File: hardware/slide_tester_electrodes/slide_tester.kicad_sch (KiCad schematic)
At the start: 17 parts, among them J1 USB_A_Stacked, J2 Conn_01x01_Male, J3 Conn_01x01_Male, Q1 C32725, Q2 C32725, Q3 C32725

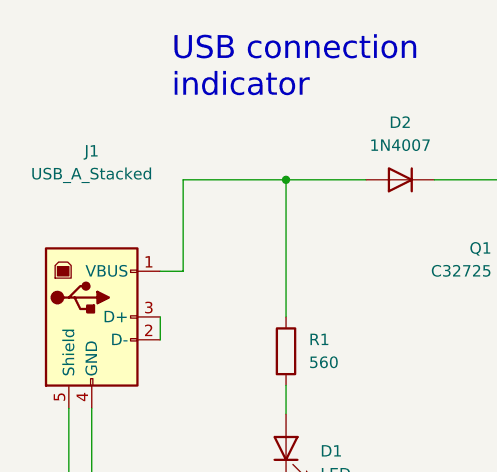
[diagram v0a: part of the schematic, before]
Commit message: Add description, figures
Add gitignore and delete back-ups
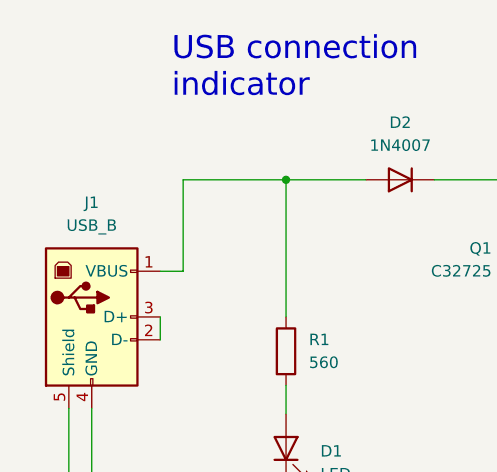
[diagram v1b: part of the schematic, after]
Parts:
- J1: value USB_A_Stacked -> USB_B
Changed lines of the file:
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@@
   (symbol (lib_id "Connector:USB_B") (at 35.56 81.28 0) (unit 1)
     (in_bom yes) (on_board yes) (fields_autoplaced)
-    (property "Reference" "J1" (id 0) (at 35.56 62.865 0))
-    (property "Value" "USB_A_Stacked" (id 1) (at 35.56 65.405 0))
+    (property "Reference" "J1" (id 0) (at 35.56 68.58 0))
+    (property "Value" "USB_B" (id 1) (at 35.56 71.12 0))
     (property "Footprint" "Connector_USB:USB_B_OST_USB-B1HSxx_Horizontal" (id 2) (at 39.37 82.55 0)
       (effects (font (size 1.27 1.27)) hide)
@@
     )
     (path "/bedc87fe-7b02-49dd-b1d2-036c65f89b7f"
-      (reference "J1") (unit 1) (value "USB_A_Stacked") (footprint "Connector_USB:USB_B_OST_USB-B1HSxx_Horizontal")
+      (reference "J1") (unit 1) (value "USB_B") (footprint "Connector_USB:USB_B_OST_USB-B1HSxx_Horizontal")
     )
     (path "/cc2c1985-993f-48d0-bedd-833f9dbf4f5d"
